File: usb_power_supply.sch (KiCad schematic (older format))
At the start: 11 parts, among them J3 Micro_USB, U4 AMS1117-3.3, U5 SRV05-4

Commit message: Replace CP2102 with CH340X
Also add BJTs to ESP32C3 strapping pins
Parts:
- removed TP1: TP_5V, TestPoint:TestPoint_Pad_D1.0mm, symbol Connector:TestPoint
- removed TP2: TP_3V3, TestPoint:TestPoint_Pad_D1.0mm, symbol Connector:TestPoint
- removed TP3: TP_GND, TestPoint:TestPoint_Pad_D1.0mm, symbol Connector:TestPoint
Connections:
- wire segments 18 -> 15
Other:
- note removed: "Test points"
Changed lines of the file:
@@
 	1    0    0    -1
 $EndComp
-$Comp
-L Connector:TestPoint TP?
-U 1 1 6382D0A1
-P 10050 1600
-AR Path="/6382D0A1" Ref="TP?"  Part="1"
-AR Path="/63818815/6382D0A1" Ref="TP1"  Part="1"
-F 0 "TP1" V 10150 1700 35  0000 C CNN
-F 1 "TP_5V" V 9950 1700 35  0000 C CNN
-F 2 "TestPoint:TestPoint_Pad_D1.0mm" H 10250 1600 50  0001 C CNN
-F 3 "~" H 10250 1600 50  0001 C CNN
-	1    10050 1600
-	0    -1   -1   0
-$EndComp
-$Comp
-L Connector:TestPoint TP?
-U 1 1 6382D0A7
-P 10050 1900
-AR Path="/6382D0A7" Ref="TP?"  Part="1"
-AR Path="/63818815/6382D0A7" Ref="TP2"  Part="1"
-F 0 "TP2" V 10150 2000 35  0000 C CNN
-F 1 "TP_3V3" V 9950 2000 35  0000 C CNN
-F 2 "TestPoint:TestPoint_Pad_D1.0mm" H 10250 1900 50  0001 C CNN
-F 3 "~" H 10250 1900 50  0001 C CNN
-	1    10050 1900
-	0    -1   -1   0
-$EndComp
-Wire Wire Line
-	10050 1600 10250 1600
-$Comp
-L power:+3.3V #PWR?
-U 1 1 6382D0AE
-P 10250 1900
-AR Path="/6382D0AE" Ref="#PWR?"  Part="1"
-AR Path="/63818815/6382D0AE" Ref="#PWR050"  Part="1"
-F 0 "#PWR050" H 10250 1750 50  0001 C CNN
-F 1 "+3.3V" H 10250 2050 35  0000 C CNN
-F 2 "" H 10250 1900 50  0001 C CNN
-F 3 "" H 10250 1900 50  0001 C CNN
-	1    10250 1900
-	1    0    0    -1
-$EndComp
-Wire Wire Line
-	10050 1900 10250 1900
-Text Notes 10750 3500 0    47   ~ 9
-Test points
-$Comp
-L power:+5V #PWR?
-U 1 1 6382D0B8
-P 10250 1600
-AR Path="/6382D0B8" Ref="#PWR?"  Part="1"
-AR Path="/63818815/6382D0B8" Ref="#PWR049"  Part="1"
-F 0 "#PWR049" H 10250 1450 50  0001 C CNN
-F 1 "+5V" H 10250 1750 35  0000 C CNN
-F 2 "" H 10250 1600 50  0001 C CNN
-F 3 "" H 10250 1600 50  0001 C CNN
-	1    10250 1600
-	1    0    0    -1
-$EndComp
-$Comp
-L power:GND #PWR?
-U 1 1 6382D0BE
-P 10250 2200
-AR Path="/6382D0BE" Ref="#PWR?"  Part="1"
-AR Path="/63818815/6382D0BE" Ref="#PWR051"  Part="1"
-F 0 "#PWR051" H 10250 1950 50  0001 C CNN
-F 1 "GND" H 10250 2050 35  0000 C CNN
-F 2 "" H 10250 2200 50  0001 C CNN
-F 3 "" H 10250 2200 50  0001 C CNN
-	1    10250 2200
-	1    0    0    -1
-$EndComp
-$Comp
-L Connector:TestPoint TP?
-U 1 1 6382D0C4
-P 10050 2200
-AR Path="/6382D0C4" Ref="TP?"  Part="1"
-AR Path="/63818815/6382D0C4" Ref="TP3"  Part="1"
-F 0 "TP3" V 10150 2300 35  0000 C CNN
-F 1 "TP_GND" V 9950 2300 35  0000 C CNN
-F 2 "TestPoint:TestPoint_Pad_D1.0mm" H 10250 2200 50  0001 C CNN
-F 3 "~" H 10250 2200 50  0001 C CNN
-	1    10050 2200
-	0    -1   -1   0
-$EndComp
-Wire Wire Line
-	10050 2200 10250 2200
 Text HLabel 1900 1850 2    35   Input ~ 0
 USB_D+
@@
 Text Notes 8050 3500 0    47   ~ 9
 USB ESD protection
-Wire Notes Line
-	500  500  11200 500
-Wire Notes Line
-	11200 500  11200 3500
-Wire Notes Line
-	11200 3500 500  3500
 Wire Notes Line
 	500  500  500  3500
@@
 Text HLabel 8100 1900 2    35   Input ~ 0
 USB_D-
+Wire Notes Line
+	500  500  8800 500
+Wire Notes Line
+	8800 3500 500  3500
 $EndSCHEMATC

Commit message: Use ESP32-C3-WROOM-02 module
Signed-off-by: Tomislav Milkovic <tomislav.milkovic95@gmail.com>
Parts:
- removed FB1: 100Ω @ 100MHz, Inductor_SMD:L_0805_2012Metric, symbol Device:Ferrite_Bead_Small
- removed J3: Micro_USB, Connector_USB:USB_Micro-B_Wuerth_629105150521, symbol Connector:USB_B_Micro
- added J4: USB_C_Receptacle_USB2.0, Connector_USB:USB_C_Receptacle_XKB_U262-16XN-4BVC11, symbol Connector:USB_C_Receptacle_USB2.0
- added R21, R22: 5K1, Resistor_SMD:R_0402_1005Metric, symbol Device:R_Small
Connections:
- net labels added: CONN_USB_D+, CONN_USB_D-
- net labels removed: 5V_USB
- wire segments 15 -> 26
- no-connect marks 2 -> 3
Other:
- note added: "USB host side capacitance limited to <= 10uF\nin order to conform to the USB2.0 specification"
- note removed: "USB host side capacitance limited to <= 10uF\nin order to conform to the USB specification"
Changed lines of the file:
@@
 $Descr A4 11693 8268
 encoding utf-8
-Sheet 5 5
+Sheet 4 5
 Title "USB connector and power suply"
 Date "2022-11-20"
@@
 Comment4 ""
 $EndDescr
-$Comp
-L Connector:USB_B_Micro J?
-U 1 1 63828FBE
-P 1600 1850
-AR Path="/63828FBE" Ref="J?"  Part="1"
-AR Path="/63818815/63828FBE" Ref="J3"  Part="1"
-F 0 "J3" H 1750 2200 35  0000 C CNN
-F 1 "Micro_USB" H 1750 1500 35  0000 C CNN
-F 2 "Connector_USB:USB_Micro-B_Wuerth_629105150521" H 1750 1800 50  0001 C CNN
-F 3 "https://datasheet.lcsc.com/lcsc/2201121330_DEALON-USB-MR-D-025_C2926996.pdf" H 1750 1800 50  0001 C CNN
-F 4 "C2926996" H 1600 1850 50  0001 C CNN "LCSC"
-	1    1600 1850
-	1    0    0    -1
-$EndComp
 $Comp
 L Regulator_Linear:AMS1117-3.3 U?
@@
 	1    0    0    -1
 $EndComp
-NoConn ~ 1900 2050
 Text Notes 2300 3500 0    47   ~ 9
 USB connector
@@
 	1    0    0    -1
 $EndComp
-$Comp
-L Device:Ferrite_Bead_Small FB?
-U 1 1 63828FFE
-P 3750 1650
-AR Path="/63828FFE" Ref="FB?"  Part="1"
-AR Path="/63818815/63828FFE" Ref="FB1"  Part="1"
-F 0 "FB1" V 3650 1700 35  0000 C CNN
-F 1 "100Ω @ 100MHz" V 3850 1600 35  0000 C CNN
-F 2 "Inductor_SMD:L_0805_2012Metric" V 3680 1650 50  0001 C CNN
-F 3 "https://datasheet.lcsc.com/lcsc/2111221630_Sunlord-GZ2012D101TF_C1015.pdf" H 3750 1650 50  0001 C CNN
-F 4 "C1015" V 3750 1650 50  0001 C CNN "LCSC"
-	1    3750 1650
-	0    1    1    0
-$EndComp
 Wire Wire Line
 	4850 1650 5050 1650
@@
 Text Notes 5650 3500 0    47   ~ 9
 5V to 3.3V LDO
-$Comp
-L power:GND #PWR?
-U 1 1 63829008
-P 1600 2250
-AR Path="/63829008" Ref="#PWR?"  Part="1"
-AR Path="/63818815/63829008" Ref="#PWR042"  Part="1"
-F 0 "#PWR042" H 1600 2000 50  0001 C CNN
-F 1 "GND" H 1600 2100 35  0000 C CNN
-F 2 "" H 1600 2250 50  0001 C CNN
-F 3 "" H 1600 2250 50  0001 C CNN
-	1    1600 2250
-	1    0    0    -1
-$EndComp
 Text Label 5550 1950 0    31   ~ 0
 PWR_LED_A
@@
 	1    0    0    -1
 $EndComp
-Wire Wire Line
-	3850 1650 3900 1650
-$Comp
-L power:PWR_FLAG #FLG?
-U 1 1 63829049
-P 3900 1650
-AR Path="/63829049" Ref="#FLG?"  Part="1"
-AR Path="/63818815/63829049" Ref="#FLG01"  Part="1"
-F 0 "#FLG01" H 3900 1725 50  0001 C CNN
-F 1 "PWR_FLAG" H 3900 1812 35  0001 C CNN
-F 2 "" H 3900 1650 50  0001 C CNN
-F 3 "~" H 3900 1650 50  0001 C CNN
-	1    3900 1650
-	1    0    0    -1
-$EndComp
-Text HLabel 1900 1850 2    35   Input ~ 0
-USB_D+
-Text HLabel 1900 1950 2    35   Input ~ 0
-USB_D-
+Text HLabel 2025 2075 2    35   Input ~ 0
+CONN_USB_D+
+Text HLabel 2025 1875 2    35   Input ~ 0
+CONN_USB_D-
 Text Notes 8050 3500 0    47   ~ 9
 USB ESD protection
@@
 	500  500  500  3500
 Wire Notes Line
-	2900 3500 2900 500
+	3075 3500 3075 500
 Wire Notes Line
 	6250 3500 6250 500
 Wire Notes Line
 	8800 3500 8800 500
-Wire Wire Line
-	3900 1650 4050 1650
-Connection ~ 3900 1650
-Wire Wire Line
-	3650 1650 3550 1650
 Wire Wire Line
 	5050 1650 5550 1650
@@
 Text Notes 5300 2500 0    35   ~ 0
 ~~1.8 mA LED current
-Text Notes 3350 2500 0    35   ~ 0
-USB host side capacitance limited to <= 10uF\nin order to conform to the USB specification
-NoConn ~ 1500 2250
-Text Label 1900 1650 0    35   ~ 0
-5V_USB
-Text Label 3550 1650 2    35   ~ 0
-5V_USB
 Text Notes 6950 2600 0    35   ~ 0
 Data lines connected to two pins for easier routing
@@
 Wire Notes Line
 	8800 3500 500  3500
+$Comp
+L Connector:USB_C_Receptacle_USB2.0 J4
+U 1 1 67B105B1
+P 1350 1925
+F 0 "J4" H 1700 2675 50  0000 C CNN
+F 1 "USB_C_Receptacle_USB2.0" H 1900 1175 50  0000 C CNN
+F 2 "Connector_USB:USB_C_Receptacle_XKB_U262-16XN-4BVC11" H 1500 1925 50  0001 C CNN
+F 3 "https://www.usb.org/sites/default/files/documents/usb_type-c.zip" H 1500 1925 50  0001 C CNN
+	1    1350 1925
+	1    0    0    -1
+$EndComp
+Wire Wire Line
+	1950 2025 1950 2075
+Wire Wire Line
+	1950 2075 2025 2075
+Wire Wire Line
+	1950 2125 1950 2075
+Connection ~ 1950 2075
+Wire Wire Line
+	1950 1825 1950 1875
+Wire Wire Line
+	1950 1875 2025 1875
+Connection ~ 1950 1875
+Wire Wire Line
+	1950 1875 1950 1925
+$Comp
+L power:GND #PWR?
+U 1 1 67B14967
+P 1350 2825
+AR Path="/67B14967" Ref="#PWR?"  Part="1"
+AR Path="/63818815/67B14967" Ref="#PWR023"  Part="1"
+F 0 "#PWR023" H 1350 2575 50  0001 C CNN
+F 1 "GND" H 1350 2675 35  0000 C CNN
+F 2 "" H 1350 2825 50  0001 C CNN
+F 3 "" H 1350 2825 50  0001 C CNN
+	1    1350 2825
+	1    0    0    -1
+$EndComp
+NoConn ~ 1050 2825
+NoConn ~ 1950 2425
+NoConn ~ 1950 2525
+Wire Wire Line
+	2525 1825 2525 1850
+Text Notes 3350 2500 0    35   ~ 0
+USB host side capacitance limited to <= 10uF\nin order to conform to the USB2.0 specification
+$Comp
+L power:+5V #PWR?
+U 1 1 67B51707
+P 1950 1325
+AR Path="/67B51707" Ref="#PWR?"  Part="1"
+AR Path="/63818815/67B51707" Ref="#PWR024"  Part="1"
+F 0 "#PWR024" H 1950 1175 50  0001 C CNN
+F 1 "+5V" H 1950 1475 35  0000 C CNN
+F 2 "" H 1950 1325 50  0001 C CNN
+F 3 "" H 1950 1325 50  0001 C CNN
+	1    1950 1325
+	1    0    0    -1
+$EndComp
+Connection ~ 2650 1850
+Wire Wire Line
+	2750 1850 2750 1825
+Wire Wire Line
+	2650 1850 2750 1850
+Wire Wire Line
+	2650 1850 2650 1900
+Wire Wire Line
+	2525 1850 2650 1850
+$Comp
+L power:GND #PWR?
+U 1 1 67B3CF8A
+P 2650 1900
+AR Path="/67B3CF8A" Ref="#PWR?"  Part="1"
+AR Path="/63818815/67B3CF8A" Ref="#PWR025"  Part="1"
+F 0 "#PWR025" H 2650 1650 50  0001 C CNN
+F 1 "GND" H 2650 1750 35  0000 C CNN
+F 2 "" H 2650 1900 50  0001 C CNN
+F 3 "" H 2650 1900 50  0001 C CNN
+	1    2650 1900
+	1    0    0    -1
+$EndComp
+Wire Wire Line
+	2750 1525 2750 1625
+$Comp
+L Device:R_Small R?
+U 1 1 67B3BFCC
+P 2750 1725
+AR Path="/67B3BFCC" Ref="R?"  Part="1"
+AR Path="/63818815/67B3BFCC" Ref="R22"  Part="1"
+F 0 "R22" H 2800 1775 35  0000 L CNN
+F 1 "5K1" H 2800 1675 35  0000 L CNN
+F 2 "Resistor_SMD:R_0402_1005Metric" H 2750 1725 50  0001 C CNN
+F 3 "https://datasheet.lcsc.com/lcsc/2206010130_UNI-ROYAL-Uniroyal-Elec-0603WAF1001T5E_C21190.pdf" H 2750 1725 50  0001 C CNN
+F 4 "C21190" H 2750 1725 50  0001 C CNN "LCSC"
+	1    2750 1725
+	1    0    0    -1
+$EndComp
+$Comp
+L Device:R_Small R?
+U 1 1 67B3A44D
+P 2525 1725
+AR Path="/67B3A44D" Ref="R?"  Part="1"
+AR Path="/63818815/67B3A44D" Ref="R21"  Part="1"
+F 0 "R21" H 2575 1775 35  0000 L CNN
+F 1 "5K1" H 2575 1675 35  0000 L CNN
+F 2 "Resistor_SMD:R_0402_1005Metric" H 2525 1725 50  0001 C CNN
+F 3 "https://datasheet.lcsc.com/lcsc/2206010130_UNI-ROYAL-Uniroyal-Elec-0603WAF1001T5E_C21190.pdf" H 2525 1725 50  0001 C CNN
+F 4 "C21190" H 2525 1725 50  0001 C CNN "LCSC"
+	1    2525 1725
+	1    0    0    -1
+$EndComp
+Wire Wire Line
+	1950 1625 2525 1625
+Wire Wire Line
+	1950 1525 2750 1525
 $EndSCHEMATC

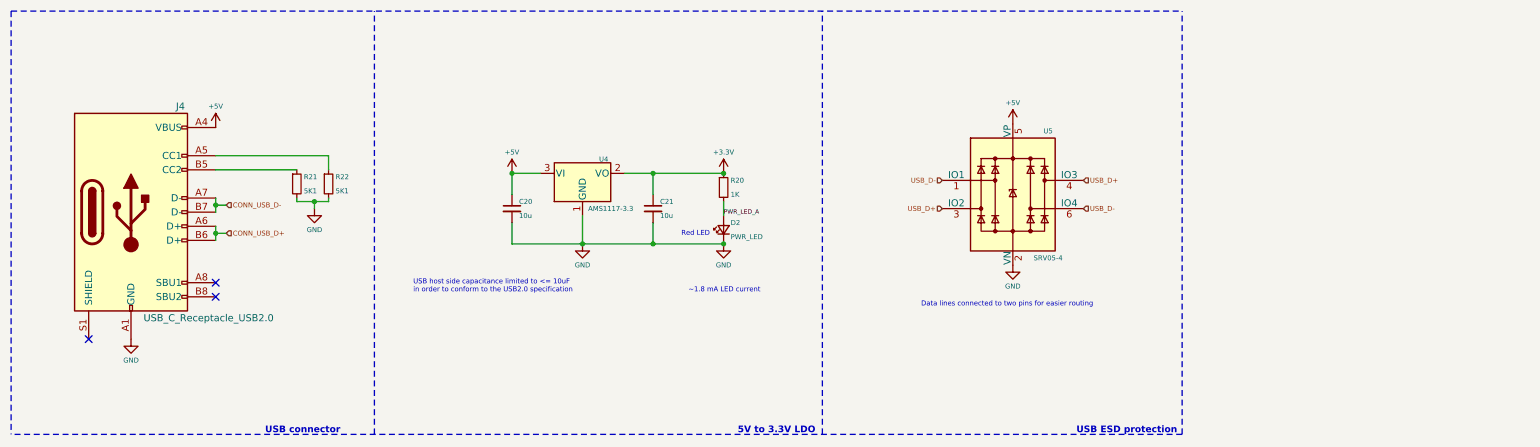
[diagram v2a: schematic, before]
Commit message: Change USB UART adapter to CP2102
Signed-off-by: Tomislav Milkovic <tomislav.milkovic95@gmail.com>
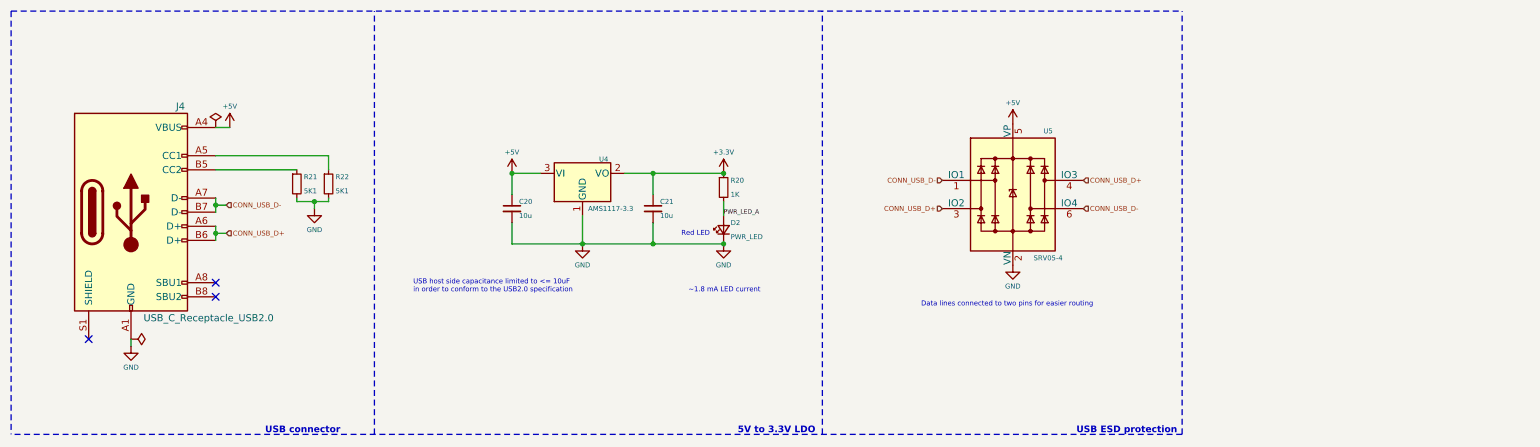
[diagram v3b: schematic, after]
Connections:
- net USB_D+ is gone; now on net CONN_USB_D+: U5.3 (IO2), U5.4 (IO3)
- net USB_D- is gone; now on net CONN_USB_D-: U5.1 (IO1), U5.6 (IO4)
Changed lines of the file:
@@
 Data lines connected to two pins for easier routing
 Text HLabel 8100 1700 2    35   Input ~ 0
-USB_D+
+CONN_USB_D+
 Text HLabel 7100 1900 0    35   Input ~ 0
-USB_D+
+CONN_USB_D+
 Text HLabel 7100 1700 0    35   Input ~ 0
-USB_D-
+CONN_USB_D-
 Text HLabel 8100 1900 2    35   Input ~ 0
-USB_D-
+CONN_USB_D-
 Wire Notes Line
 	500  500  8800 500
@@
 L power:GND #PWR?
 U 1 1 67B14967
-P 1350 2825
+P 1350 2875
 AR Path="/67B14967" Ref="#PWR?"  Part="1"
 AR Path="/63818815/67B14967" Ref="#PWR023"  Part="1"
-F 0 "#PWR023" H 1350 2575 50  0001 C CNN
-F 1 "GND" H 1350 2675 35  0000 C CNN
-F 2 "" H 1350 2825 50  0001 C CNN
-F 3 "" H 1350 2825 50  0001 C CNN
-	1    1350 2825
+F 0 "#PWR023" H 1350 2625 50  0001 C CNN
+F 1 "GND" H 1350 2725 35  0000 C CNN
+F 2 "" H 1350 2875 50  0001 C CNN
+F 3 "" H 1350 2875 50  0001 C CNN
+	1    1350 2875
 	1    0    0    -1
 $EndComp
@@
 L power:+5V #PWR?
 U 1 1 67B51707
-P 1950 1325
+P 2050 1325
 AR Path="/67B51707" Ref="#PWR?"  Part="1"
 AR Path="/63818815/67B51707" Ref="#PWR024"  Part="1"
-F 0 "#PWR024" H 1950 1175 50  0001 C CNN
-F 1 "+5V" H 1950 1475 35  0000 C CNN
-F 2 "" H 1950 1325 50  0001 C CNN
-F 3 "" H 1950 1325 50  0001 C CNN
-	1    1950 1325
+F 0 "#PWR024" H 2050 1175 50  0001 C CNN
+F 1 "+5V" H 2050 1475 35  0000 C CNN
+F 2 "" H 2050 1325 50  0001 C CNN
+F 3 "" H 2050 1325 50  0001 C CNN
+	1    2050 1325
 	1    0    0    -1
 $EndComp
@@
 Wire Wire Line
 	1950 1525 2750 1525
+$Comp
+L power:PWR_FLAG #FLG0101
+U 1 1 67B3EC81
+P 1950 1325
+F 0 "#FLG0101" H 1950 1400 50  0001 C CNN
+F 1 "PWR_FLAG" H 1950 1498 50  0001 C CNN
+F 2 "" H 1950 1325 50  0001 C CNN
+F 3 "~" H 1950 1325 50  0001 C CNN
+	1    1950 1325
+	1    0    0    -1
+$EndComp
+$Comp
+L power:PWR_FLAG #FLG0102
+U 1 1 67B3F8E1
+P 1350 2825
+F 0 "#FLG0102" H 1350 2900 50  0001 C CNN
+F 1 "PWR_FLAG" H 1350 2998 50  0001 C CNN
+F 2 "" H 1350 2825 50  0001 C CNN
+F 3 "~" H 1350 2825 50  0001 C CNN
+	1    1350 2825
+	0    1    1    0
+$EndComp
+Wire Wire Line
+	1350 2875 1350 2825
+Wire Wire Line
+	1950 1325 2050 1325
 $EndSCHEMATC

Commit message: Add LCSC part numbers for all components
Signed-off-by: Tomislav Milkovic <tomislav.milkovic95@gmail.com>
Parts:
- C20, C21: footprint Capacitor_SMD:C_0805_2012Metric -> Capacitor_SMD:C_0603_1608Metric; LCSC C12891 -> C19702
- J4: LCSC (none) -> C393939
- R20: footprint Resistor_SMD:R_0603_1608Metric -> Resistor_SMD:R_0402_1005Metric; LCSC C21190 -> C11702
- R21, R22: LCSC C21190 -> C25905
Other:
- note added: "~~1.3 mA LED current"
- note removed: "~~1.8 mA LED current"
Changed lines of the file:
@@
 Sheet 4 5
 Title "USB connector and power suply"
-Date "2022-11-20"
+Date "2025-02-16"
 Rev "1.0"
 Comp "Copyright: Tomislav Milkovic"
@@
 F 1 "AMS1117-3.3" H 4750 1400 35  0000 C CNN
 F 2 "Package_TO_SOT_SMD:SOT-223-3_TabPin2" H 4550 1850 50  0001 C CNN
-F 3 "https://datasheet.lcsc.com/lcsc/1811142212_Advanced-Monolithic-Systems-AMS1117-3-3_C6186.pdf" H 4650 1400 50  0001 C CNN
+F 3 "https://jlcpcb.com/api/file/downloadByFileSystemAccessId/8550724073479806976" H 4650 1400 50  0001 C CNN
 F 4 "C6186" H 4550 1650 50  0001 C CNN "LCSC"
 	1    4550 1650
@@
 F 0 "C20" H 4100 1950 35  0000 L CNN
 F 1 "10u" H 4100 1850 35  0000 L CNN
-F 2 "Capacitor_SMD:C_0805_2012Metric" H 4050 1900 50  0001 C CNN
-F 3 "https://datasheet.lcsc.com/lcsc/1811031514_Samsung-Electro-Mechanics-CL31A226KAHNNNE_C12891.pdf" H 4050 1900 50  0001 C CNN
-F 4 "C12891" H 4050 1900 50  0001 C CNN "LCSC"
+F 2 "Capacitor_SMD:C_0603_1608Metric" H 4050 1900 50  0001 C CNN
+F 3 "https://www.lcsc.com/datasheet/lcsc_datasheet_2304140030_Samsung-Electro-Mechanics-CL10A106KP8NNNC_C19702.pdf" H 4050 1900 50  0001 C CNN
+F 4 "C19702" H 4050 1900 50  0001 C CNN "LCSC"
 	1    4050 1900
 	1    0    0    -1
@@
 F 0 "C21" H 5100 1950 35  0000 L CNN
 F 1 "10u" H 5100 1850 35  0000 L CNN
-F 2 "Capacitor_SMD:C_0805_2012Metric" H 5050 1900 50  0001 C CNN
-F 3 "https://datasheet.lcsc.com/lcsc/1811031514_Samsung-Electro-Mechanics-CL31A226KAHNNNE_C12891.pdf" H 5050 1900 50  0001 C CNN
-F 4 "C12891" H 5050 1900 50  0001 C CNN "LCSC"
+F 2 "Capacitor_SMD:C_0603_1608Metric" H 5050 1900 50  0001 C CNN
+F 3 "https://www.lcsc.com/datasheet/lcsc_datasheet_2304140030_Samsung-Electro-Mechanics-CL10A106KP8NNNC_C19702.pdf" H 5050 1900 50  0001 C CNN
+F 4 "C19702" H 5050 1900 50  0001 C CNN "LCSC"
 	1    5050 1900
 	1    0    0    -1
@@
 F 1 "PWR_LED" V 5500 2000 35  0000 R CNN
 F 2 "LED_SMD:LED_0603_1608Metric" V 5550 2050 50  0001 C CNN
-F 3 "https://datasheet.lcsc.com/lcsc/1810231112_Hubei-KENTO-Elec-KT-0603R_C2286.pdf" V 5550 2050 50  0001 C CNN
+F 3 "https://jlcpcb.com/api/file/downloadByFileSystemAccessId/8550723991833485312" V 5550 2050 50  0001 C CNN
 F 4 "C2286" V 5550 2050 50  0001 C CNN "LCSC"
 	1    5550 2050
@@
 F 0 "R20" H 5600 1800 35  0000 L CNN
 F 1 "1K" H 5600 1700 35  0000 L CNN
-F 2 "Resistor_SMD:R_0603_1608Metric" H 5550 1750 50  0001 C CNN
-F 3 "https://datasheet.lcsc.com/lcsc/2206010130_UNI-ROYAL-Uniroyal-Elec-0603WAF1001T5E_C21190.pdf" H 5550 1750 50  0001 C CNN
-F 4 "C21190" H 5550 1750 50  0001 C CNN "LCSC"
+F 2 "Resistor_SMD:R_0402_1005Metric" H 5550 1750 50  0001 C CNN
+F 3 "https://www.lcsc.com/datasheet/lcsc_datasheet_2206010216_UNI-ROYAL-Uniroyal-Elec-0402WGF1001TCE_C11702.pdf" H 5550 1750 50  0001 C CNN
+F 4 "C11702" H 5550 1750 50  0001 C CNN "LCSC"
 	1    5550 1750
 	1    0    0    -1
@@
 F 1 "SRV05-4" H 7850 1350 35  0000 C CNN
 F 2 "Package_TO_SOT_SMD:SOT-23-6" H 8300 1350 50  0001 C CNN
-F 3 "https://datasheet.lcsc.com/lcsc/1809192313_ProTek-Devices-SRV05-4-P-T7_C85364.pdf" H 7600 1800 50  0001 C CNN
+F 3 "https://www.lcsc.com/datasheet/lcsc_datasheet_1809192313_ProTek-Devices-SRV05-4-P-T7_C85364.pdf" H 7600 1800 50  0001 C CNN
 F 4 "C85364" H 7600 1800 50  0001 C CNN "LCSC"
 	1    7600 1800
@@
 Connection ~ 5550 2150
 Text Notes 5300 2500 0    35   ~ 0
-~~1.8 mA LED current
+~~1.3 mA LED current
 Text Notes 6950 2600 0    35   ~ 0
 Data lines connected to two pins for easier routing
@@
 F 1 "USB_C_Receptacle_USB2.0" H 1900 1175 50  0000 C CNN
 F 2 "Connector_USB:USB_C_Receptacle_XKB_U262-16XN-4BVC11" H 1500 1925 50  0001 C CNN
-F 3 "https://www.usb.org/sites/default/files/documents/usb_type-c.zip" H 1500 1925 50  0001 C CNN
+F 3 "https://www.lcsc.com/datasheet/lcsc_datasheet_1912111437_SHOU-HAN-TYPE-C16PIN_C393939.pdf" H 1500 1925 50  0001 C CNN
+F 4 "C393939" H 1350 1925 50  0001 C CNN "LCSC"
 	1    1350 1925
 	1    0    0    -1
@@
 F 1 "5K1" H 2800 1675 35  0000 L CNN
 F 2 "Resistor_SMD:R_0402_1005Metric" H 2750 1725 50  0001 C CNN
-F 3 "https://datasheet.lcsc.com/lcsc/2206010130_UNI-ROYAL-Uniroyal-Elec-0603WAF1001T5E_C21190.pdf" H 2750 1725 50  0001 C CNN
-F 4 "C21190" H 2750 1725 50  0001 C CNN "LCSC"
+F 3 "https://www.lcsc.com/datasheet/lcsc_datasheet_2206010045_UNI-ROYAL-Uniroyal-Elec-0402WGF5101TCE_C25905.pdf" H 2750 1725 50  0001 C CNN
+F 4 "C25905" H 2750 1725 50  0001 C CNN "LCSC"
 	1    2750 1725
 	1    0    0    -1
@@
 F 1 "5K1" H 2575 1675 35  0000 L CNN
 F 2 "Resistor_SMD:R_0402_1005Metric" H 2525 1725 50  0001 C CNN
-F 3 "https://datasheet.lcsc.com/lcsc/2206010130_UNI-ROYAL-Uniroyal-Elec-0603WAF1001T5E_C21190.pdf" H 2525 1725 50  0001 C CNN
-F 4 "C21190" H 2525 1725 50  0001 C CNN "LCSC"
+F 3 "https://www.lcsc.com/datasheet/lcsc_datasheet_2206010045_UNI-ROYAL-Uniroyal-Elec-0402WGF5101TCE_C25905.pdf" H 2525 1725 50  0001 C CNN
+F 4 "C25905" H 2525 1725 50  0001 C CNN "LCSC"
 	1    2525 1725
 	1    0    0    -1
